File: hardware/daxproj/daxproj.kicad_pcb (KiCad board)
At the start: 2 copper layers, 77 parts, among them J2 6437288-1, J3 JTAG, Q1 Q_PMOS_GDS, Q2 MBT3904DW1T1G, Q3 MBT3904DW1T1G, Q4 MBT3904DW1T1G, SW1 SW_Push, U1 TPS5430DDA, U2 SN65HVD230, U3 STM32F103C8T6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

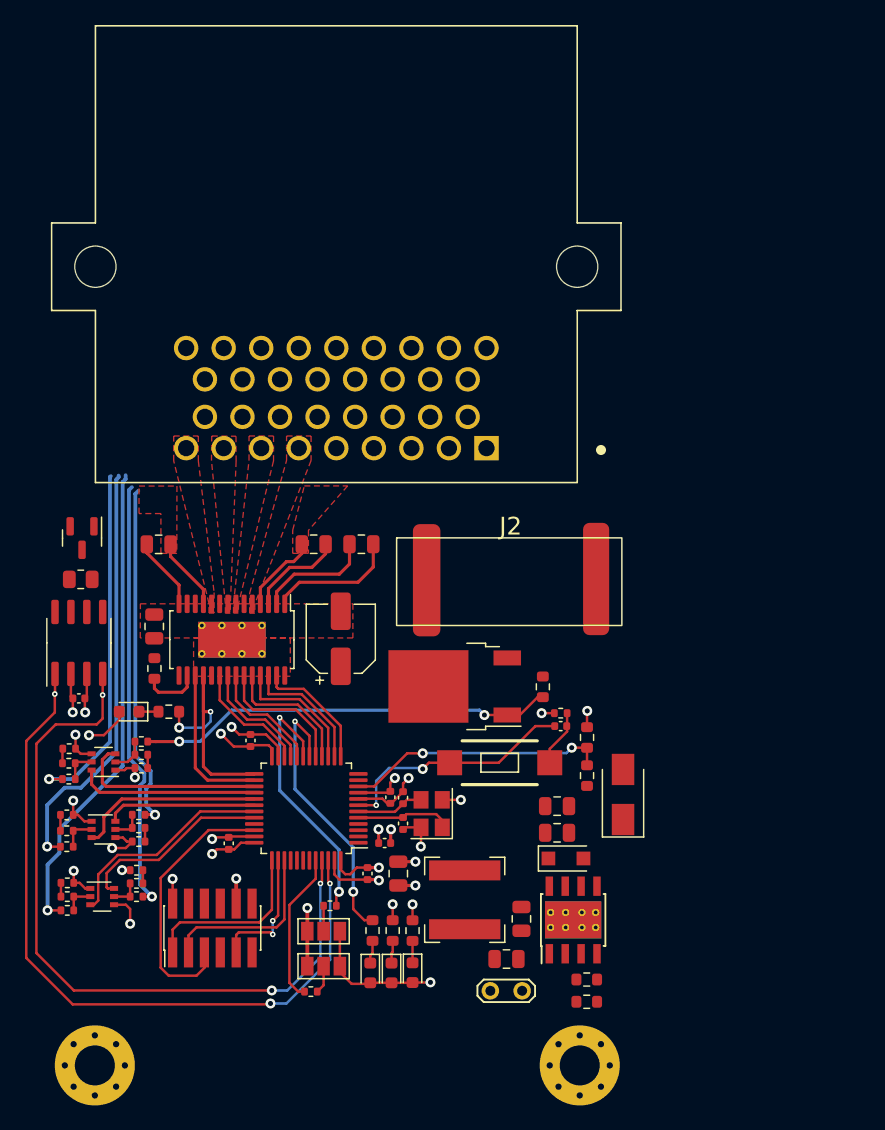
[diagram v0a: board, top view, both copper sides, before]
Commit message: Finish routing motor controller board
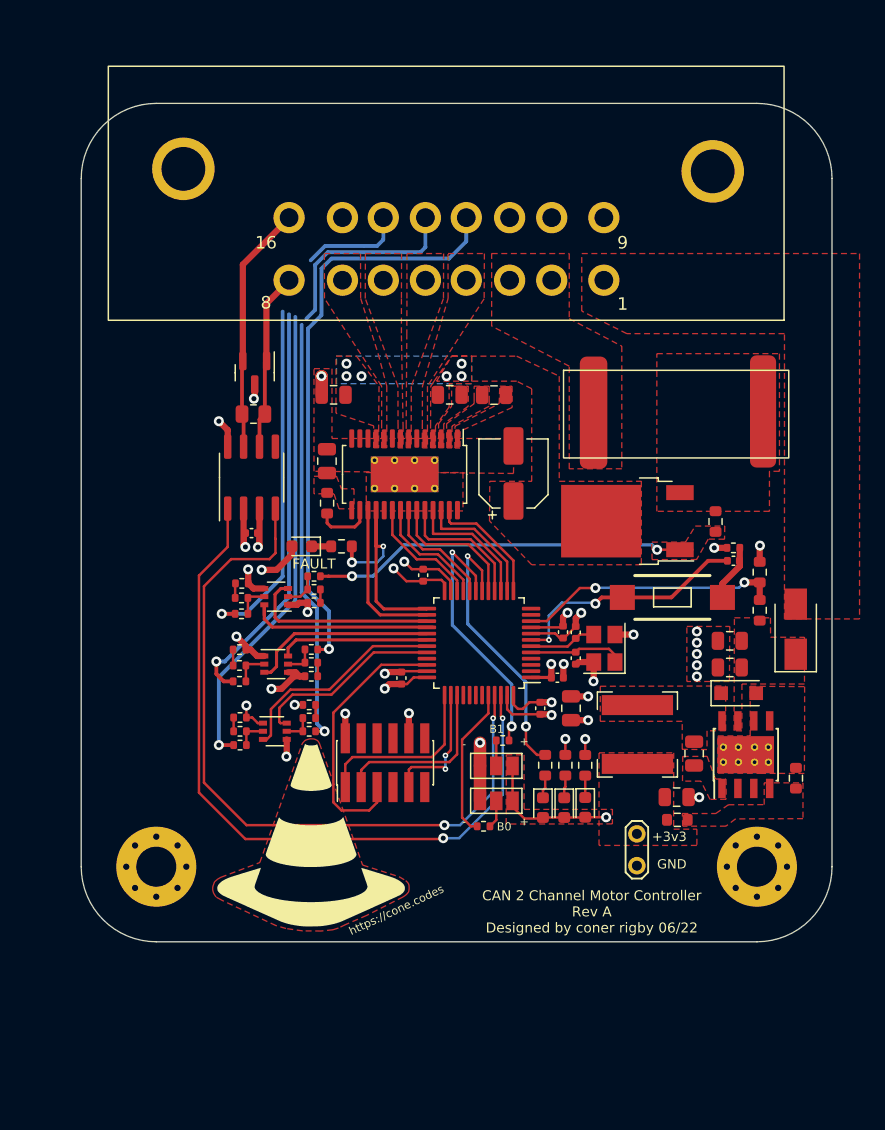
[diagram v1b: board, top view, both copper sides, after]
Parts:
- added G***: LOGO, logos:cone, F.Cu at (38.4, 81.5)
- J2: value 6437288-1 -> Conn_02x08_Top_Bottom; footprint ConeCodes:6437288-1 -> ConeCodes:953371
- moved R5 24.5 mm to (77.1, 76.9), turned to 90 degrees
- moved J2 23.1 mm to (49.2, 25.2)
- moved H2 21.3 mm to (74.0, 84.0)
- moved C12 19.1 mm to (59.5, 67.3)
- moved C13 19.1 mm to (59.5, 65.3)
- moved C3 19.1 mm to (69.0, 75.0)
- moved R12 19.1 mm to (52.2, 80.8)
- moved R6 19.1 mm to (60.3, 75.9)
- moved J3 19.1 mm to (44.3, 75.7)
- moved R26 19.1 mm to (32.8, 63.8)
- moved R27 19.1 mm to (38.4, 67.7)
- moved C11 19.1 mm to (45.6, 68.9)
- moved C17 19.1 mm to (54.5, 52.6)
- moved C2 19.1 mm to (71.8, 68.1)
- moved C9 19.1 mm to (47.3, 60.7)
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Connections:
- net /VM renamed /12VOUT
- D7 pad 1: /CAN_P -> /CANL
- D7 pad 2: /CAN_N -> /CANH
- J2 pad 12: unconnected-(J2-Pad12) -> /GPI1
- J2 pad 16: unconnected-(J2-Pad16) -> /CANH
- J2 pad 3: /GPI3 -> /VBAT_IN
- J2 pad 4: /GPI4 -> /MOTOR1_OUT1
- J2 pad 5: unconnected-(J2-Pad5) -> /MOTOR1_OUT2
- J2 pad 6: /MOTOR1_OUT1 -> /MOTOR2_OUT1
- J2 pad 7: /MOTOR1_OUT2 -> /MOTOR2_OUT2
- J2 pad 8: /MOTOR2_OUT1 -> /CANL
- J2 pad 9: /MOTOR2_OUT2 -> unconnected-(J2-Pad9)
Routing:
- net /CANH: track 0.00 -> 19.9 mm
- net /GPI1: track 28.4 -> 47.5 mm
- net unconnected-(J2-Pad13): track 0.00 -> 16.3 mm
- net /CANL: track 0.00 -> 14.3 mm
- net /12VOUT: track 12.3 -> 0.00 mm, vias 0 -> 6
- net /CP1: track 10.4 -> 0.00 mm
- net /CP2: track 9.29 -> 0.00 mm
- net unconnected-(J2-Pad14): track 0.00 -> 8.25 mm
- net /VCP: track 7.70 -> 0.00 mm
- net +3V3: track 38.2 -> 43.2 mm
- net GND: track 64.2 -> 67.6 mm, vias 22 -> 31
- net /VOUT_EN: track 33.4 -> 31.0 mm
- net /GPI2: track 33.8 -> 33.1 mm
- net /GPI3: track 34.6 -> 34.0 mm
- net /CANRX: track 59.2 -> 59.5 mm, vias 3 -> 2
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- added copper zone on F.Cu, net (none)
- added copper zone on F.Cu, net +12V
- added copper zone on F.Cu, net +3V3
- added copper zone on In2.Cu, net +3V3
- added copper zone on B.Cu, net /12VOUT
- added copper zone on F.Cu, net /BOOT
- added copper zone on F.Cu, net /CP1
- added copper zone on F.Cu, net /CP2
- added copper zone on F.Cu, net /FUSED_VBAT_IN
- added copper zone on F.Cu, net /PH
- added copper zone on F.Cu, net /V3P3OUT
- added copper zone on F.Cu, net /VBAT_IN
- added copper zone on F.Cu, net /VCP
- added copper zone on F.Cu, net /VIN
- added copper zone on F.Cu, net /VOUT_EN
- added copper zone on F.Cu, net /VSENSE
- added copper zone on In1.Cu, net GND
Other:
- board outline added: 60 x 67 mm
- copper layers 2 -> 4
- board text added: "+"
- board text added: "+3v3"
- board text added: "-"
- board text added: "B0"
- board text added: "B1"
- board text added: "CAN 2 Channel Motor Controller Rev A Designed by coner rigby 06/22"
- board text added: "FAULT"
- board text added: "GND"
- board text added: "https://cone.codes"
